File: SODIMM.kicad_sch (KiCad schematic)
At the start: 3 parts, among them CN1 YXT-BB10-50P-02, CN2 YXT-BB10-50P-02, CN3 YXT-BB10-50P-02

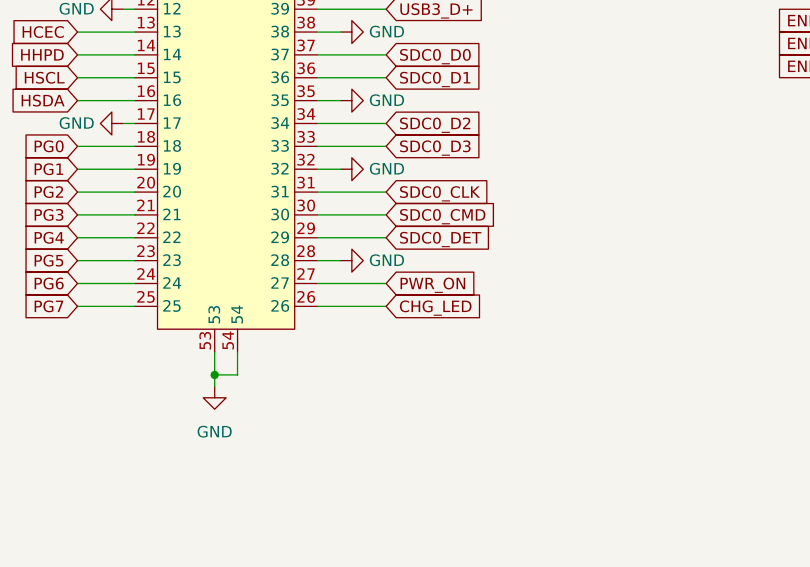
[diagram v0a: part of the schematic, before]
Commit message: power routing additions
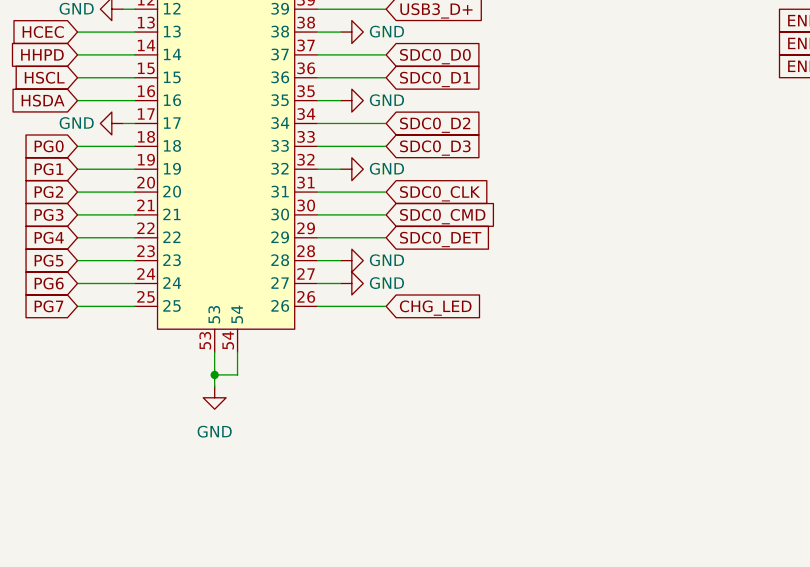
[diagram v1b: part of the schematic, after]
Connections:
- net GND: now also CN1.27
- net PWR_ON: no longer CN1.27
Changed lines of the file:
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@@
 	(wire
 		(pts
-			(xy 110.49 138.43) (xy 118.11 138.43)
-		)
-		(stroke
-			(width 0)
-			(type default)
-		)
-	)
-	(wire
-		(pts
 			(xy 209.55 96.52) (xy 203.2 96.52)
 		)
@@
 	(wire
 		(pts
+			(xy 113.03 138.43) (xy 110.49 138.43)
+		)
+		(stroke
+			(width 0)
+			(type default)
+		)
+	)
+	(wire
+		(pts
 			(xy 156.21 226.06) (xy 166.37 226.06)
 		)
@@
 		)
 	)
-	(global_label "PWR_ON"
-		(shape input)
-		(at 118.11 138.43 0)
-		(fields_autoplaced yes)
-		(effects
-			(font
-				(size 1.27 1.27)
-			)
-			(justify left)
-		)
-		(property "Intersheetrefs" "${INTERSHEET_REFS}"
-			(at 128.7152 138.43 0)
-			(effects
-				(font
-					(size 1.27 1.27)
-				)
-				(justify left)
-				(hide yes)
-			)
-		)
-	)
 	(global_label "MICIN_2-"
 		(shape input)
@@
 					(unit 1)
 				)
+			)
+		)
+	)
+	(symbol
+		(lib_id "power:GND")
+		(at 113.03 138.43 90)
+		(mirror x)
+		(unit 1)
+		(exclude_from_sim no)
+		(in_bom yes)
+		(on_board yes)
+		(dnp no)
+		(fields_autoplaced yes)
+		(property "Reference" "#PWR078"
+			(at 119.38 138.43 0)
+			(effects
+				(font
+					(size 1.27 1.27)
+				)
+				(hide yes)
+			)
+		)
+		(property "Value" "GND"
+			(at 116.205 138.43 90)
+			(effects
+				(font
+					(size 1.27 1.27)
+				)
+				(justify right)
+			)
+		)
+		(property "Footprint" ""
+			(at 113.03 138.43 0)
+			(effects
+				(font
+					(size 1.27 1.27)
+				)
+				(hide yes)
+			)
+		)
+		(property "Datasheet" ""
+			(at 113.03 138.43 0)
+			(effects
+				(font
+					(size 1.27 1.27)
+				)
+				(hide yes)
+			)
+		)
+		(property "Description" ""
+			(at 113.03 138.43 0)
+			(effects
+				(font
+					(size 1.27 1.27)
+				)
+			)
+		)
+		(pin "1"
+		)
+		(instances
+			(project "H3_SBC"
+				(path "/2511caf5-b791-49bc-bcf7-734707cf883b/820235b6-3e55-4f19-988b-04cbfedf3fbe"
+					(reference "#PWR078")
+					(unit 1)
+				)

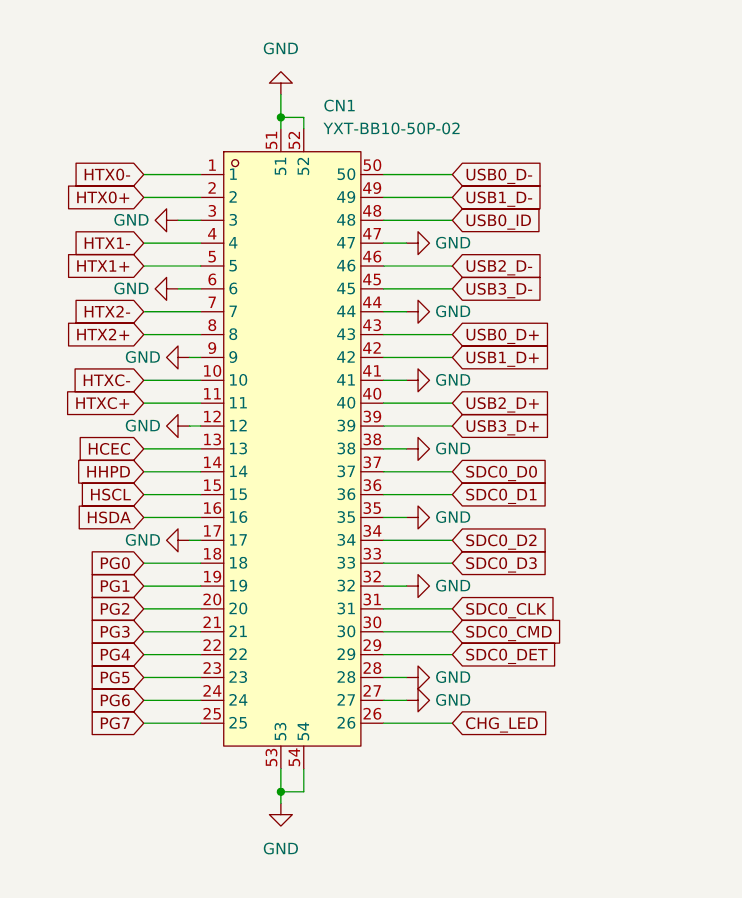
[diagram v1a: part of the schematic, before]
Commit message: placed all decaps, emmc routing changes, DDR routing changes
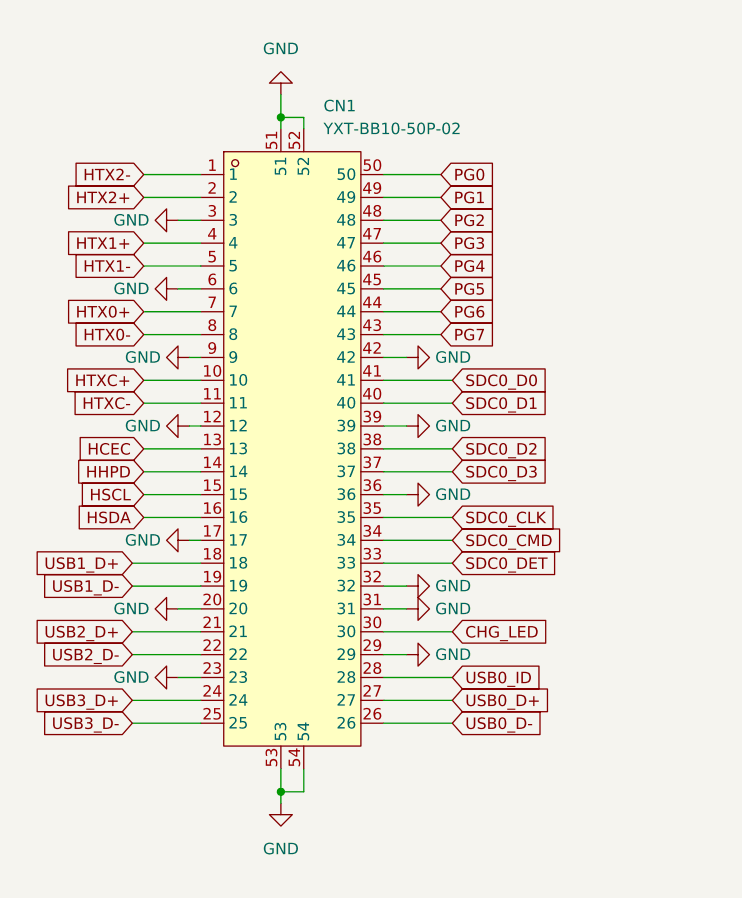
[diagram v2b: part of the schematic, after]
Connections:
- net CHG_LED: now also CN1.30; no longer CN1.26
- net GND: now also CN1.20, CN1.23, CN1.29, CN1.31, CN1.36, CN1.39, CN1.42; no longer CN1.27, CN1.28, CN1.35, CN1.38, CN1.41, CN1.44, CN1.47
- net HTX0+: now also CN1.7; no longer CN1.2
- net HTX0-: now also CN1.8; no longer CN1.1
- net HTX1+: now also CN1.4; no longer CN1.5
- net HTX1-: now also CN1.5; no longer CN1.4
- net HTX2+: now also CN1.2; no longer CN1.8
- net HTX2-: now also CN1.1; no longer CN1.7
- net HTXC+: now also CN1.10; no longer CN1.11
- net HTXC-: now also CN1.11; no longer CN1.10
- net PG0: now also CN1.50; no longer CN1.18
- net PG1: now also CN1.49; no longer CN1.19
- net PG2: now also CN1.48; no longer CN1.20
- net PG3: now also CN1.47; no longer CN1.21
- net PG4: now also CN1.46; no longer CN1.22
- net PG5: now also CN1.45; no longer CN1.23
- net PG6: now also CN1.44; no longer CN1.24
- net PG7: now also CN1.43; no longer CN1.25
- net SDC0_CLK: now also CN1.35; no longer CN1.31
- net SDC0_CMD: now also CN1.34; no longer CN1.30
- net SDC0_D0: now also CN1.41; no longer CN1.37
- net SDC0_D1: now also CN1.40; no longer CN1.36
- net SDC0_D2: now also CN1.38; no longer CN1.34
- net SDC0_D3: now also CN1.37; no longer CN1.33
- net SDC0_DET: now also CN1.33; no longer CN1.29
- net USB0_D+: now also CN1.27; no longer CN1.43
- net USB0_D-: now also CN1.26; no longer CN1.50
- net USB0_ID: now also CN1.28; no longer CN1.48
- net USB1_D+: now also CN1.18; no longer CN1.42
- net USB1_D-: now also CN1.19; no longer CN1.49
- net USB2_D+: now also CN1.21; no longer CN1.40
- net USB2_D-: now also CN1.22; no longer CN1.46
- net USB3_D+: now also CN1.24; no longer CN1.39
- net USB3_D-: now also CN1.25; no longer CN1.45
